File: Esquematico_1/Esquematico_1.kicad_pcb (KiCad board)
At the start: 6 copper layers, 116.8 x 46.1 mm, 93 parts, among them IC1 AP2112K-3.3TRG1, J1 Screw_Terminal_01x04, J2 Screw_Terminal_01x03, J3 Screw_Terminal_01x06, J4 Screw_Terminal_01x08, J5 SWD, J6 Screw_Terminal_01x04, J7 USB_C_Receptacle_USB2.0_16P, U1 ICM-42688-P, U2 STM32F405RGTx, U3 Mag, U4 BMP388, U5 USBLC6-2SC6, U6 TPS54302DDCR

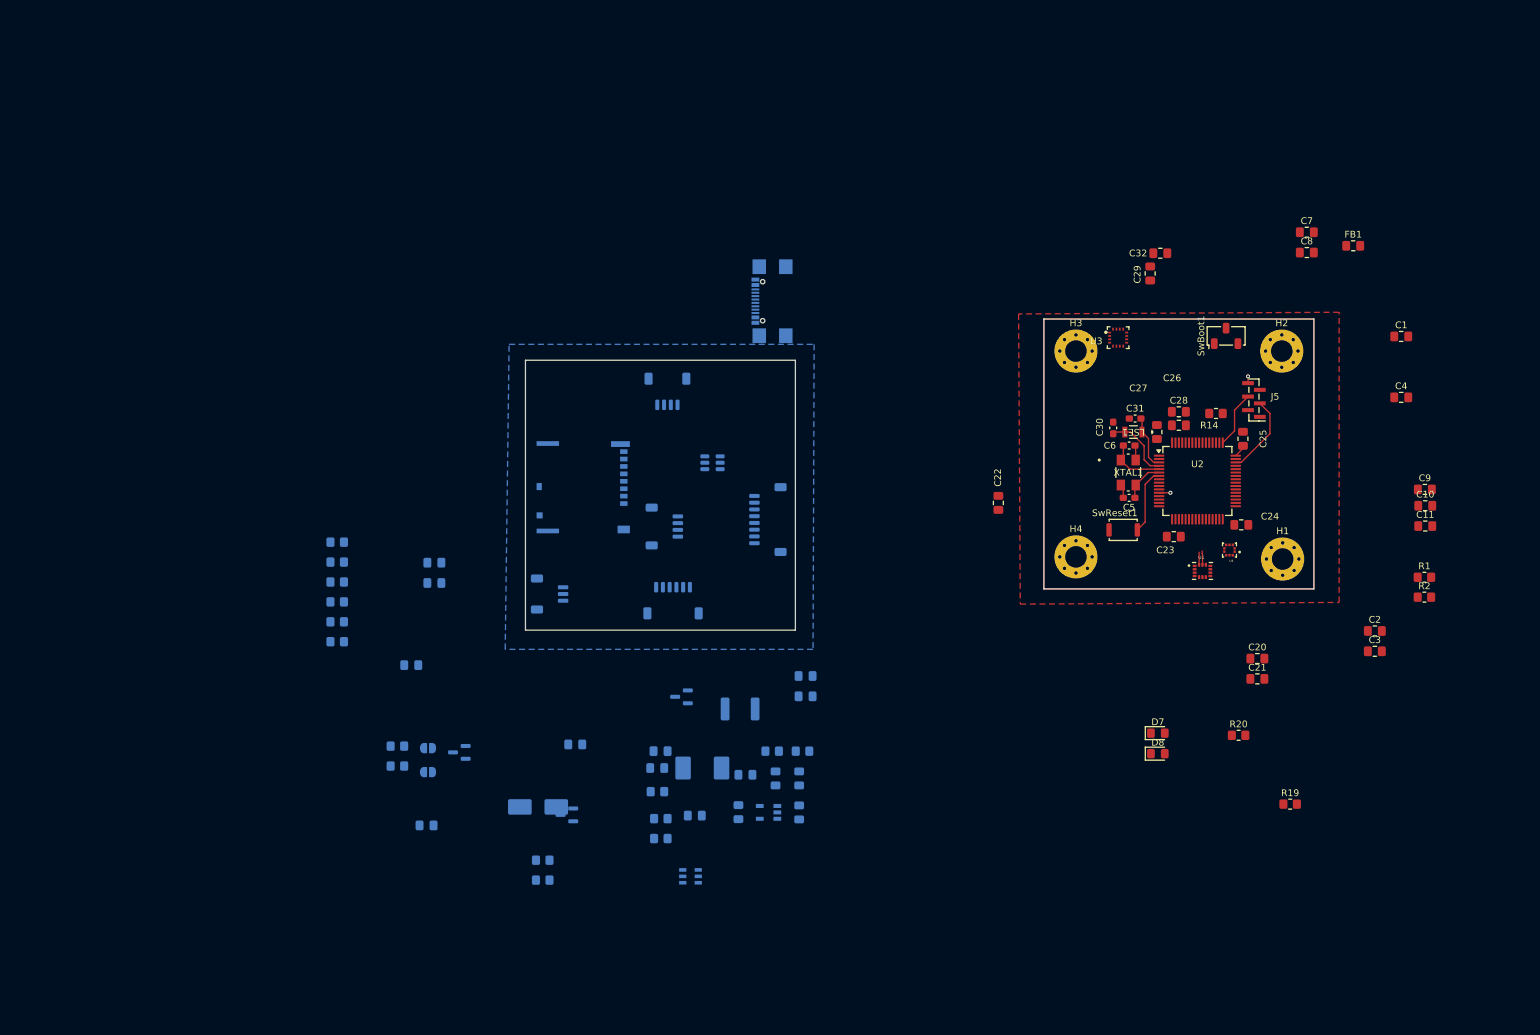
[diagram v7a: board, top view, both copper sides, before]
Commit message: Update PCB backlayer
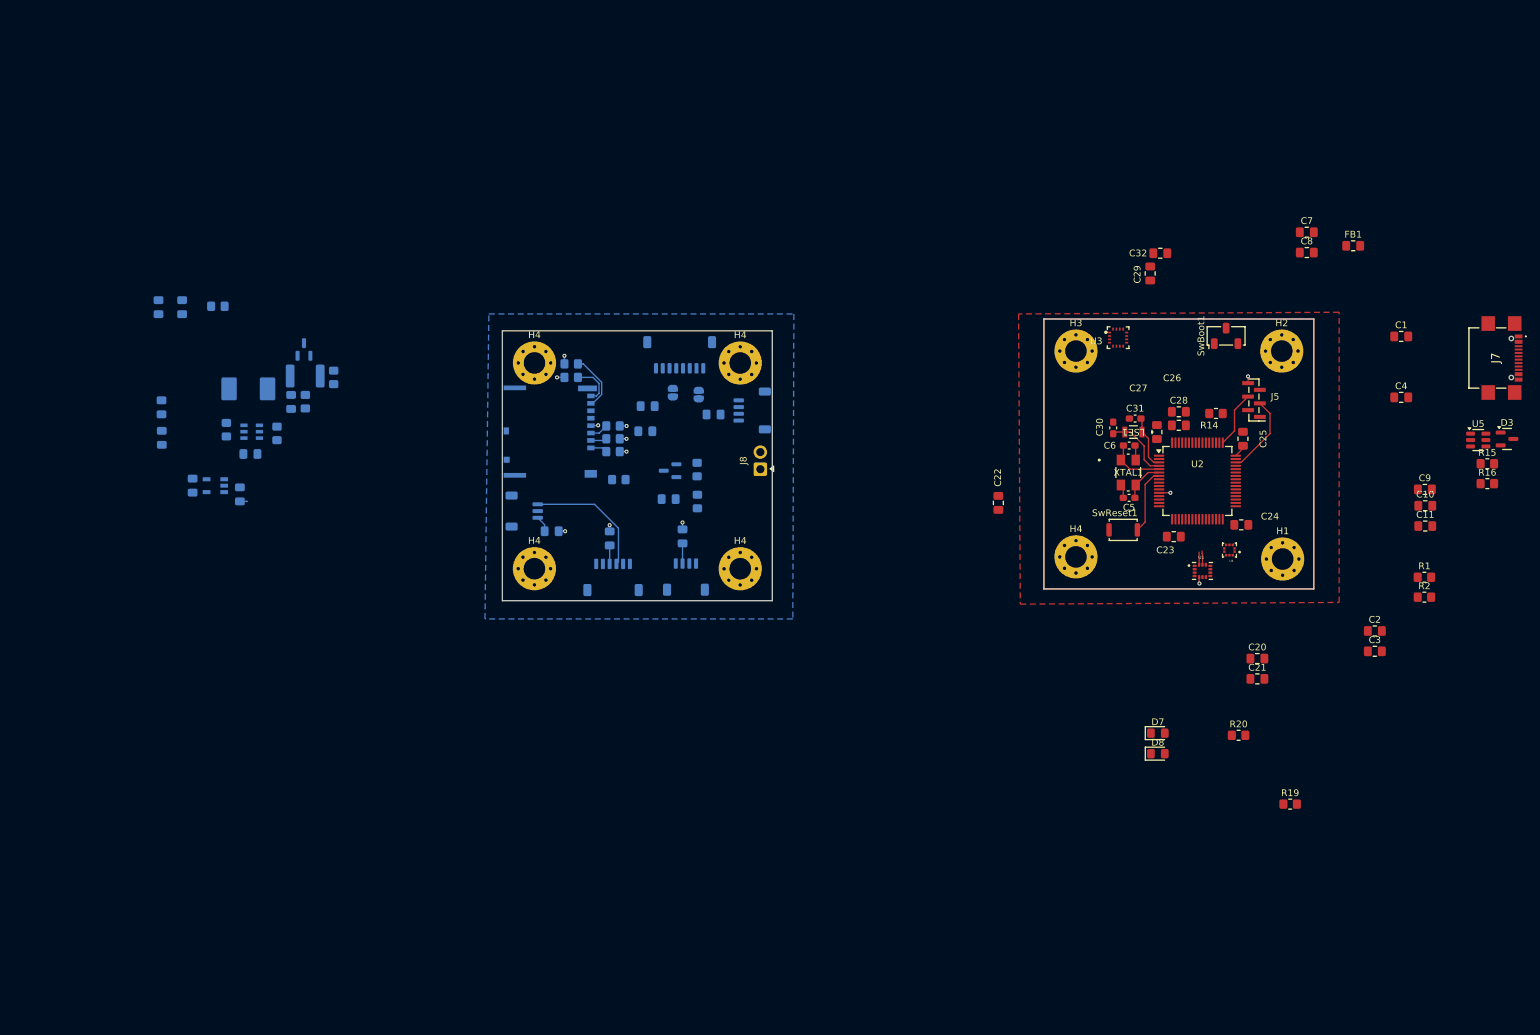
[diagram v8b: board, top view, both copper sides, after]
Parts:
- removed D2: TVS, Diode_SMD:D_SMB_Handsoldering
- added H4: MountingHole, MountingHole:MountingHole_3.2mm_M3_Pad_Via, F.Cu at (94.8, 76.8)
- added H4: MountingHole, MountingHole:MountingHole_3.2mm_M3_Pad_Via, F.Cu at (125.2, 76.8)
- added H4: MountingHole, MountingHole:MountingHole_3.2mm_M3_Pad_Via, F.Cu at (125.2, 107.3)
- added H4: MountingHole, MountingHole:MountingHole_3.2mm_M3_Pad_Via, F.Cu at (94.8, 107.2)
- added J8: Screw_Terminal_01x02, TerminalBlock:TerminalBlock_Xinya_XY308-2.54-2P_1x02_P2.54mm_Horizontal, F.Cu at (128.2, 92.5)
- D3, J7, R15, R16, U5: moved to F.Cu
- moved R15 166.9 mm to (236.0, 91.7), turned to 0 degrees
- moved R16 166.9 mm to (236.0, 94.6), turned to 0 degrees
- moved D3 162.1 mm to (238.9, 88.0), turned to 0 degrees
- moved C13 115.1 mm to (42.5, 68.5)
- moved C14 115.1 mm to (39.0, 68.5)
- moved U5 113.5 mm to (234.6, 88.2)
- moved J7 106.1 mm to (236.9, 76.0)
- moved R9 105.3 mm to (47.8, 68.4)
- moved R10 97.8 mm to (49.1, 86.7), turned to 90 degrees
- moved C18 95.3 mm to (51.1, 96.2), turned to -90 degrees
- moved IC1 95.2 mm to (47.5, 95.0)
- moved C19 94.3 mm to (44.1, 94.9), turned to 90 degrees
- moved U6 92.6 mm to (52.9, 87.0), turned to 90 degrees
- moved C16 89.8 mm to (39.5, 83.3), turned to -90 degrees
- moved C17 88.2 mm to (39.5, 87.9), turned to -90 degrees
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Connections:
- C13 pad 2: Vbat -> VCC
- C14 pad 2: Vbat -> VCC
- R17 pad 1: Vbat -> VCC
- R9 pad 2: Vbat -> VCC
- U6 pad 3: Vbat -> VCC
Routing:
- net VIDEO: track 0.00 -> 18.8 mm
- net SDIO_D0: track 0.00 -> 8.59 mm
- net +3V3: track 1.91 -> 9.38 mm, vias 0 -> 7
- net SDIO_D1: track 0.00 -> 6.31 mm
- net LDO_USB: track 0.00 -> 4.02 mm, vias 0 -> 3
- net Net-(J1-Pin_3): track 0.00 -> 2.99 mm
- net Net-(J3-Pin_4): track 0.00 -> 2.74 mm
- net SDIO_CMD: track 0.00 -> 2.72 mm
- net SDIO_D2: track 0.00 -> 2.51 mm
- net Net-(J2-Pin_1): track 0.00 -> 2.41 mm
- net SDIO_D3: track 0.00 -> 2.39 mm
- added copper zone on In3.Cu, net +3V3
- added copper zone on In3.Cu, net LDO_USB
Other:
- board size 116.8 x 46.1 mm -> 120.2 x 41.8 mm
